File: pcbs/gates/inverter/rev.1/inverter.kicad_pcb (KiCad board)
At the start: 2 copper layers, 7.6 x 7.6 mm, 6 parts, among them J1 Conn_01x03, J2 Conn_01x03, Q1 BSS84, Q2 2N7002

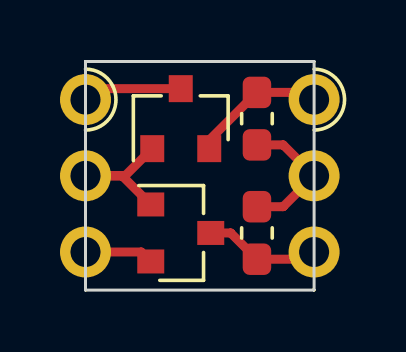
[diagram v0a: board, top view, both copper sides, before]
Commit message: re-organized project directory and started work on ALU pcb
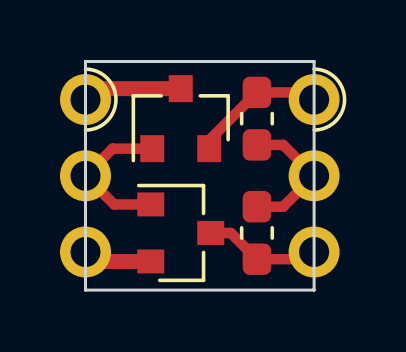
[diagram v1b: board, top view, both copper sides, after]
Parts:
- moved J1 7.62 mm to (86.4, 50.8)
- moved J2 7.62 mm to (94.0, 50.8)
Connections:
- J1 pad 1: Pti -> Vdd
- J1 pad 2: Out -> In
- J1 pad 3: Nti -> Vss
- J2 pad 1: Vdd -> Pti
- J2 pad 2: In -> Out
- J2 pad 3: Vss -> Nti
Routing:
- net In: track 5.17 -> 3.97 mm
- net Out: track 4.66 -> 3.46 mm
- net Vss: track 2.31 -> 1.67 mm
